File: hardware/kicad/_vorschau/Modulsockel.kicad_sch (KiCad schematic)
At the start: 16 parts, among them J100 Stapelstecker 2x20, J101 Kettenstecker, Buchse oben (S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, J102 Kettenstecker, Stift unten (S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, J103 Leistungsstecker, Buchse oben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, J104 Leistungsstecker, Stift unten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, U100 STM32C011F6P6, U101 SN74LVC1G175, U102 SN74LVC2G00DCUR, U103 SN74LVC1G08

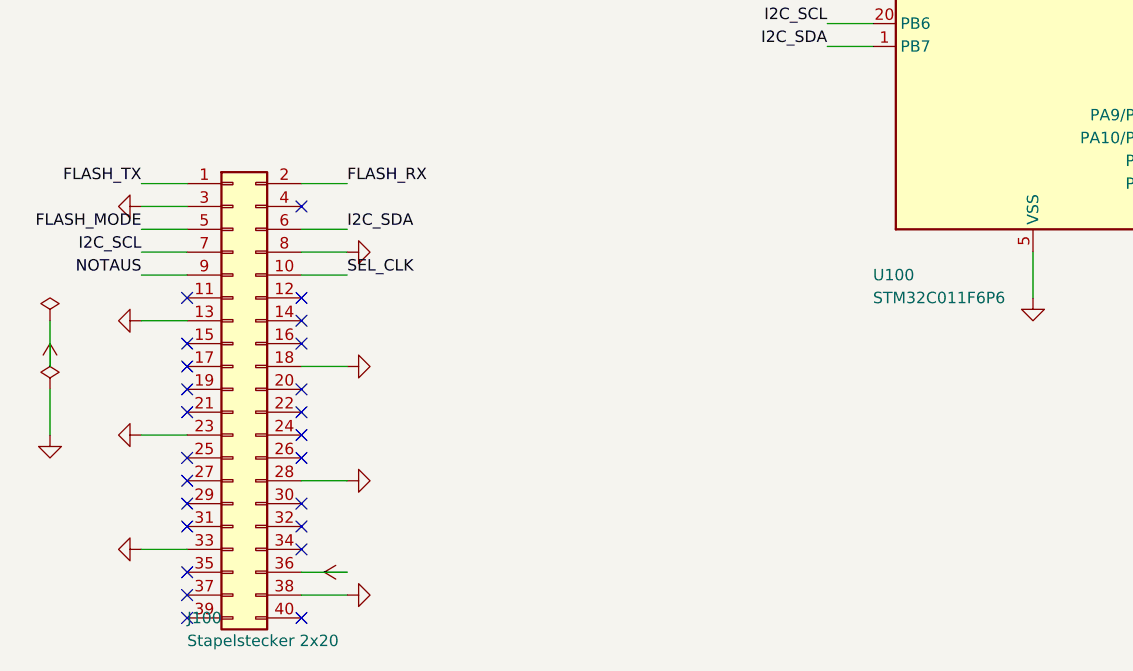
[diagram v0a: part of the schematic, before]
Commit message: Aufgabe 4: gen.py MPN-Felder + modulsockel.py v2 (Stapelreihen, Randpads)
gen.Schaltplan.bauteil() bekommt einen optionalen felder=-Parameter
(dict zusaetzlicher Symbol-Properties wie LCSC/MPN, spaeter gebraucht
fuer Stuecklisten-Aufgaben) -- parallel gespeichert (self.FELDER,
gleicher Index wie COMPS), nicht als zehntes COMPS-Feld, aus demselben
Grund wie beim bestehenden dnp-Flag. felder=None aendert die Ausgabe
nicht (verifiziert).

modulsockel._stapelstecker() zerlegt den frueheren 2x20-Block in zwei
1x20-Buchsenreihen (STECKER_POS["stapel_links"/"stapel_rechts"],
Footprints jetzt aus dem Vertrag statt lokal dupliziert) -- Signatur
jetzt (sch, ref_links, ref_rechts, ox, oy, frei_durchreichen=False).
Pico-Pin-Formel: Kontakt k auf ref_links == Pico-Pin k, Kontakt k auf
ref_rechts == Pico-Pin k+20; jede Pin-Rolle bleibt woertlich wie in v1
verdrahtet, nur ueber zwei Referenzen verteilt. einbauen() ruft jetzt
J100 (links) + J105 (rechts).

Neue Funktion modulsockel.randpads(): platziert J95 (18 GPIO-Loetpads)
und J96 (2x 3V3 + 2x GND) nach stack_spec.RANDPADS, beide unbestueckt
(dnp=True). Unabhaengig von einbauen() -- ein Board verbindet Randpad
und freien Stapel-Pin allein durch gleichlautende Netznamen (kein
gemeinsamer Draht noetig), verdrahtet also beide Funktionen mit
frei_durchreichen=True, wenn es die Kante tatsaechlich speisen will.

TDD: tests/test_modulsockel.py zuerst umgeschrieben (RED gegen die
unveraenderte v1-Fassung nachgewiesen: KeyError 'J105' beim Aufbau der
Modulseiten-Pruefung), dann implementiert bis GREEN. Empirisch mit
kicad-cli 10.0.6 gegengeprueft: die ERC-Warnungszahl von einbauen()
(0 Fehler, 6 isolated_pin_label-Warnungen) bleibt unveraendert, weil
beide Steckersymbole denselben Pin-Typ (passive) tragen.

Rot-Liste waechst gegenueber der Baseline (test_erzeugte_dateien,
test_spec_dimmer, test_spec_motor, test_spec_sockel) um zwei erlaubte,
temporaere Eintraege -- beide direkte Konsumenten der alten
Einreihen-Signatur, Migration ist Tas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
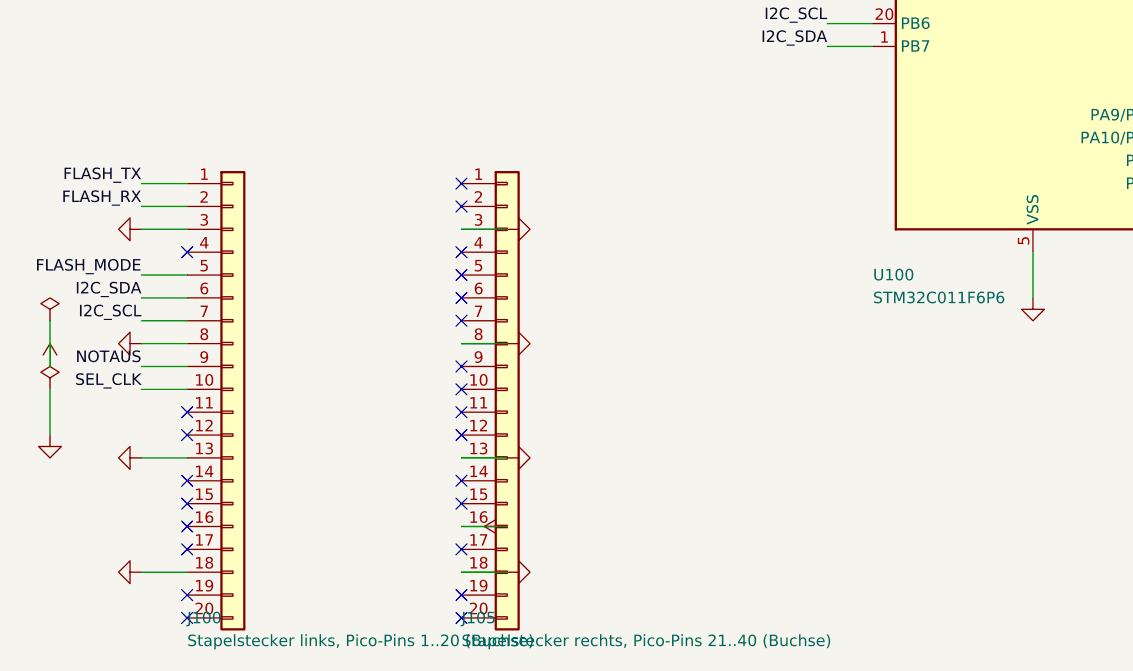
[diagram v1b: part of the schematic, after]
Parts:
- added R101: Kennwiderstand (Modultyp), Resistor_SMD:R_0805_2012Metric_Pad1.20x1.40mm_HandSolder, symbol Device:R
- C100: renamed from U101; value SN74LVC1G175 -> 100n; footprint Package_TO_SOT_SMD:SOT-363_SC-70-6 -> Capacitor_SMD:C_0805_2012Metric_Pad1.18x1.45mm_HandSolder; symbol 74xGxx:74LVC1G175 -> Device:C
- C101: renamed from U102; value SN74LVC2G00DCUR -> 1000n; footprint Package_SO:VSSOP-8_2.3x2mm_P0.5mm -> Capacitor_SMD:C_0805_2012Metric_Pad1.18x1.45mm_HandSolder; symbol 74xGxx:74LVC2G00 -> Device:C
- J100: value Stapelstecker 2x20 -> Stapelstecker links, Pico-Pins 1..20 (Buchse); footprint Connector_PinHeader_2.54mm:PinHeader_2x20_P2.54mm_Vertical -> Connector_PinSocket_2.54mm:PinSocket_1x20_P2.54mm_Vertical; symbol Connector_Generic:Conn_02x20_Odd_Even -> Connector_Generic:Conn_01x20
- J101: renamed from J102; value Kettenstecker, Stift unten (SMD) -> Kettenstecker, Buchse oben (SMD); footprint Connector_PinHeader_2.54mm:PinHeader_1x02_P2.54mm_Vertical_SMD_Pin1Left -> Connector_PinSocket_2.54mm:PinSocket_1x02_P2.54mm_Vertical_SMD_Pin1Left
- J102: renamed from J103; value Leistungsstecker, Buchse oben (SMD) -> Kettenstecker, Stift unten (SMD); footprint Connector_PinSocket_2.54mm:PinSocket_2x02_P2.54mm_Vertical_SMD -> Connector_PinHeader_2.54mm:PinHeader_1x02_P2.54mm_Vertical_SMD_Pin1Left; symbol Connector_Generic:Conn_02x02_Odd_Even -> Connector_Generic:Conn_01x02
- J103: renamed from J104; value Leistungsstecker, Stift unten (SMD) -> Leistungsstecker, Buchse oben (SMD); footprint Connector_PinHeader_2.54mm:PinHeader_2x02_P2.54mm_Vertical_SMD -> Connector_PinSocket_2.54mm:PinSocket_2x02_P2.54mm_Vertical_SMD
- J104: renamed from U100; value STM32C011F6P6 -> Leistungsstecker, Stift unten (SMD); footprint Package_SO:TSSOP-20_4.4x6.5mm_P0.65mm -> Connector_PinHeader_2.54mm:PinHeader_2x02_P2.54mm_Vertical_SMD; symbol MCU_ST_STM32C0:STM32C011F6Px -> Connector_Generic:Conn_02x02_Odd_Even
- J105: renamed from J101; value Kettenstecker, Buchse oben (SMD) -> Stapelstecker rechts, Pico-Pins 21..40 (Buchse); footprint Connector_PinSocket_2.54mm:PinSocket_1x02_P2.54mm_Vertical_SMD_Pin1Left -> Connector_PinSocket_2.54mm:PinSocket_1x20_P2.54mm_Vertical; symbol Connector_Generic:Conn_01x02 -> Connector_Generic:Conn_01x20
- R100: renamed from R105; value 10000 (ID_OBEN) -> Kennwiderstand (Modultyp)
- R102: renamed from C101; value 1000n -> 100k; footprint Capacitor_SMD:C_0805_2012Metric_Pad1.18x1.45mm_HandSolder -> Resistor_SMD:R_0805_2012Metric_Pad1.20x1.40mm_HandSolder; symbol Device:C -> Device:R
- R104: renamed from R100; value Kennwiderstand (Modultyp) -> 10000 (ID_OBEN)
- R105: renamed from R101; value Kennwiderstand (Modultyp) -> 10000 (ID_OBEN)
- U100: renamed from C100; value 100n -> STM32C011F6P6; footprint Capacitor_SMD:C_0805_2012Metric_Pad1.18x1.45mm_HandSolder -> Package_SO:TSSOP-20_4.4x6.5mm_P0.65mm; symbol Device:C -> MCU_ST_STM32C0:STM32C011F6Px
- U101: renamed from R102; value 100k -> SN74LVC1G175; footprint Resistor_SMD:R_0805_2012Metric_Pad1.20x1.40mm_HandSolder -> Package_TO_SOT_SMD:SOT-363_SC-70-6; symbol Device:R -> 74xGxx:74LVC1G175
- U102: renamed from U103; value SN74LVC1G08 -> SN74LVC2G00DCUR; footprint Package_TO_SOT_SMD:SOT-353_SC-70-5 -> Package_SO:VSSOP-8_2.3x2mm_P0.5mm; symbol 74xGxx:74LVC1G08 -> 74xGxx:74LVC2G00
- U103: renamed from R104; value 10000 (ID_OBEN) -> SN74LVC1G08; footprint Resistor_SMD:R_0805_2012Metric_Pad1.20x1.40mm_HandSolder -> Package_TO_SOT_SMD:SOT-353_SC-70-5; symbol Device:R -> 74xGxx:74LVC1G08
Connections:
- net 3V3: now also C100.1, C101.2, J104.2 (Pin_2), J105.13 (Pin_13), J105.16 (Pin_16), J105.18 (Pin_18), J105.3 (Pin_3), J105.8 (Pin_8), R100.2, R102.1, R104.1, R105.1, U100.4 (VDD), U100.5 (VSS), U101.2 (GND), U101.5 (VCC), U102.4 (GND), U102.8 (VCC), U103.3 (GND), U103.5 (VCC), R101.2; no longer C100.5 (VCC), J100.23 (Pin_23), J100.28 (Pin_28), J100.33 (Pin_33), J100.36 (Pin_36), J100.38 (Pin_38), J102.4 (Pin_4), J104.5 (VSS), J105.2 (Pin_2), R100.1, R102.2, R104.2, R105.2, U100.1, U100.2, U101.1, U102.3 (GND), U102.4 (GND), U102.5 (VCC), U102.8 (VCC), U103.1
- net BOOT0: now also U100.19 (PA14), U103.4; no longer J104.19 (PA14), U102.4
- net FLASH_MODE: now also U102.5, U103.1; no longer U102.1, U102.5
- net FLASH_RX: now also U100.16 (PA9/PA11); no longer J104.16 (PA9/PA11)
- net FLASH_TX: now also U100.17 (PA10/PA12); no longer J104.17 (PA10/PA12)
- net I2C_SCL: now also U100.20 (PB6); no longer J104.20 (PB6)
- net I2C_SDA: now also U100.1 (PB7); no longer J104.1 (PB7)
- net ID0: now also R100.1, R104.2, U100.7 (PA0); no longer J104.7 (PA0), R104.1, U103.2
- net ID1: now also R105.2, U100.8 (PA1), R101.1; no longer J104.8 (PA1), R100.2, R105.1
- net IN1: now also U100.9 (PA2); no longer J104.9 (PA2)
- net IN2: now also U100.10 (PA3); no longer J104.10 (PA3)
- net IPROPI: now also U100.13 (PA6); no longer J104.13 (PA6)
- net NCLR: now also C101.1, R102.2, U101.6 (~{CLR}); no longer C100.6 (~{CLR}), R102.1, U101.2
- net NFAULT: now also U100.12 (PA5); no longer J104.12 (PA5)
- net NQ: now also U102.6, U102.7; no longer C101.7, U102.6
- net NRST: now also U100.6 (PF2), U102.3; no longer J104.6 (PF2), U102.3
- net NSLEEP: now also U100.11 (PA4); no longer J104.11 (PA4)
- net PWR24V: now also J104.1 (Pin_1), J104.3 (Pin_3); no longer J102.1 (Pin_1), J102.3 (Pin_3)
- net SEL_CLK: now also U101.1 (C); no longer C100.1 (C)
- net SEL_IN: now also J101.1 (Pin_1), U101.3 (D); no longer C100.3 (D), J105.1 (Pin_1)
- net SEL_OUT: now also J102.1 (Pin_1), U101.4 (Q), U102.1, U102.2, U103.2; no longer C100.4 (Q), C101.1, C101.2, J101.1 (Pin_1), U102.2
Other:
- moved on the sheet: J101, J103, R100, R104, R105, U102A
